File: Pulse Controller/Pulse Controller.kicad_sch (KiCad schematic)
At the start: 24 parts, among them J1 Serial, J2 RGB LED, J3 Arduino Out 1, J4 Arduino Out 2, J5 MOSFET Gates, J6 To ADC Board, P1 CONN_2, P2 PushButton, U1 ZSR330GTA, U2 ZSR500GTA, U3 4N35, U4 23LC1024

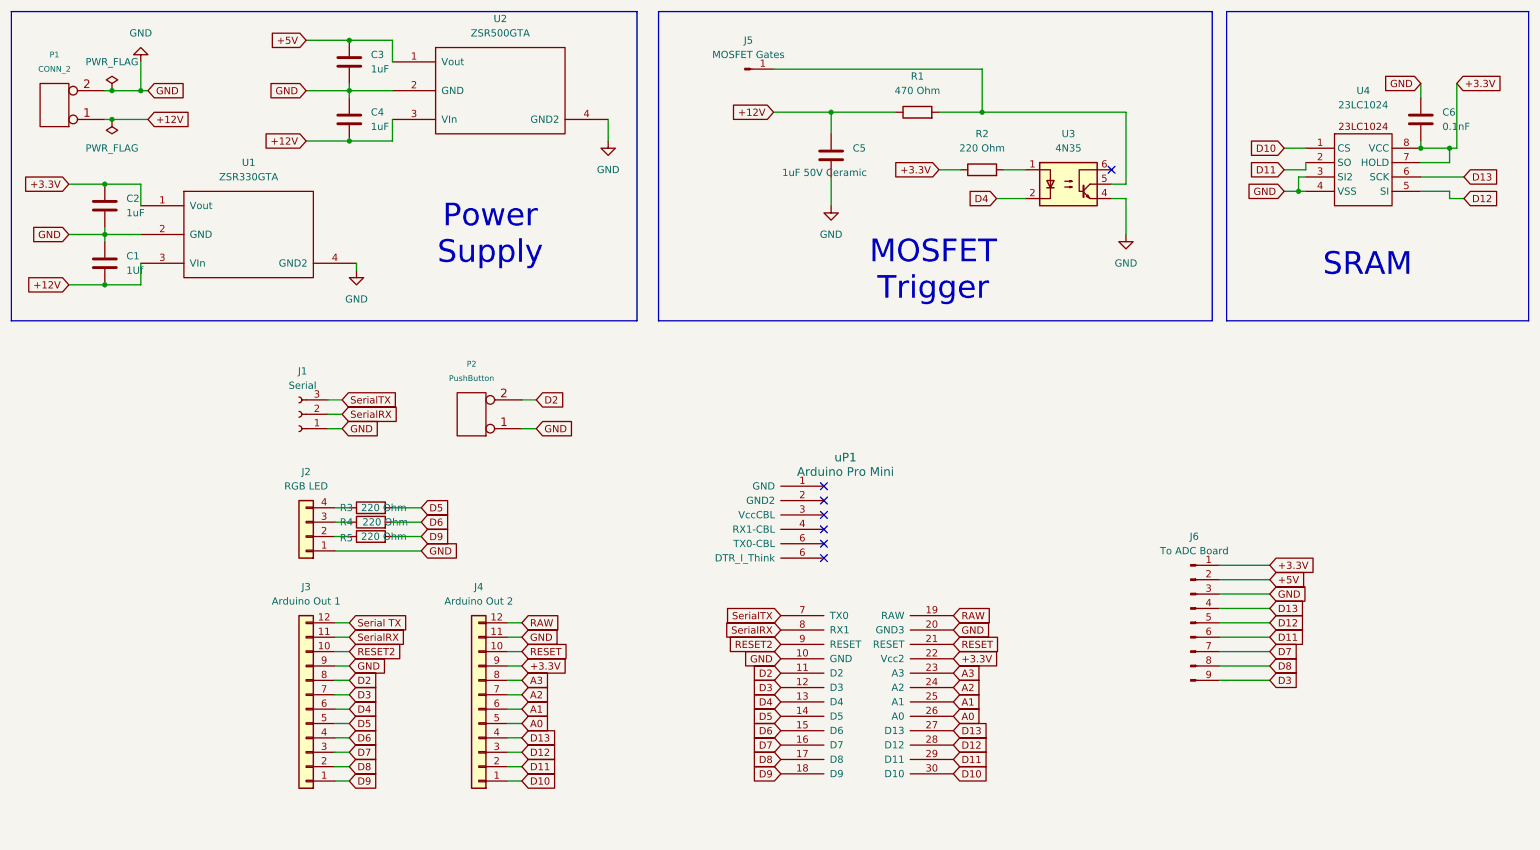
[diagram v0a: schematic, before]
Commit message: V1.0 of PPM Pulse Controller
Combined with ADC for analysis
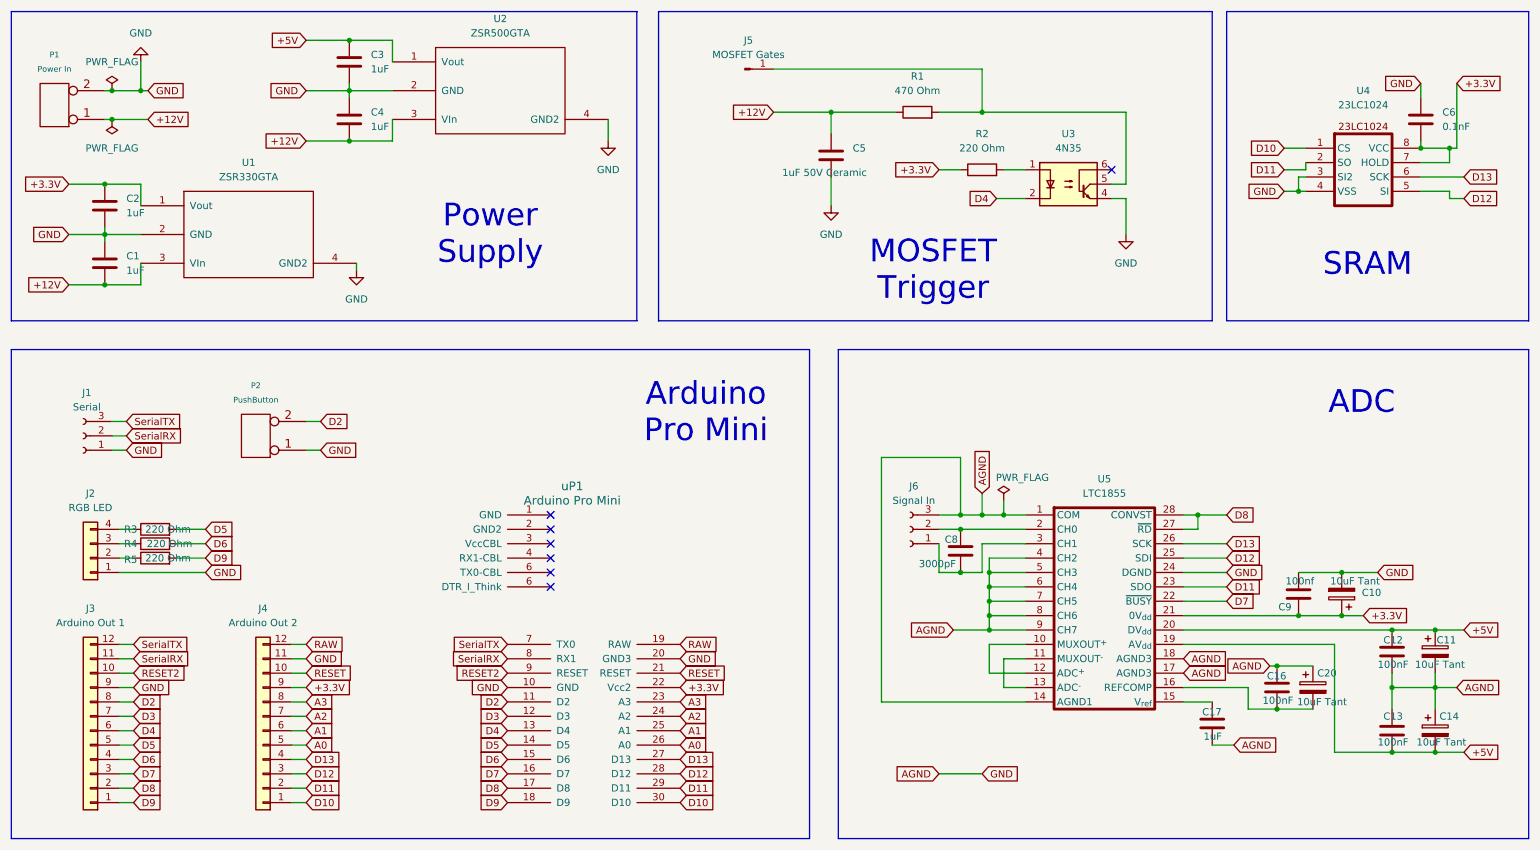
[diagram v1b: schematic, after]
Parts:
- removed J6: To ADC Board, Connector_PinHeader_2.54mm:PinHeader_1x09_P2.54mm_Vertical, symbol Connector:Conn_01x09_Pin
- added C10, C11, C14, C20: 10uF Tant, Capacitor_THT:C_Disc_D5.0mm_W2.5mm_P2.50mm, symbol Device:C_Polarized
- added C12, C13, C16: 100nF, Capacitor_SMD:C_0805_2012Metric_Pad1.18x1.45mm_HandSolder, symbol Device:C
- added C17: 1uF, Capacitor_SMD:C_0805_2012Metric_Pad1.18x1.45mm_HandSolder, symbol Device:C
- added C8: 3000pF, Capacitor_SMD:C_0805_2012Metric_Pad1.18x1.45mm_HandSolder, symbol Device:C
- added C9: 100nf, Capacitor_SMD:C_0805_2012Metric_Pad1.18x1.45mm_HandSolder, symbol Device:C
- added J6: Signal In, Connector_PinHeader_2.54mm:PinHeader_1x03_P2.54mm_Vertical, symbol Connector:Conn_01x03_Socket
- added U5: LTC1855, Package_SO:SSOP-28_5.3x10.2mm_P0.65mm, symbol DQM:LTC1855
- C1: value 1Uf -> 1uF
- C5: footprint Capacitor_THT:CP_Radial_D8.0mm_P3.50mm -> Capacitor_THT:C_Disc_D5.0mm_W2.5mm_P2.50mm
- J5: footprint DQM:PIN_ARRAY_1 -> Connector_PinHeader_2.54mm:PinHeader_1x01_P2.54mm_Horizontal
- P1: value CONN_2 -> Power In
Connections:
- net Serial TX is gone; now on net SerialTX: J3.12 (Pin_12)
- net +3.3V: now also C10.1, C9.2, U5.21 (0V_{dd})
- net +5V: now also C11.1, C12.1, C13.2, C14.2, U5.19 (AV_{dd}), U5.20 (DV_{dd})
- net D11: now also U5.23 (SDO)
- net D12: now also U5.25 (SDI)
- net D13: now also U5.26 (SCK)
- net D7: now also U5.22 (~{BUSY})
- net D8: now also U5.27 (~{RD}), U5.28 (CONVST)
- net GND: now also C10.2, C11.2, C12.2, C13.1, C14.1, C16.1, C17.2, C20.1, C9.1, J6.3 (Pin_3), U5.1 (COM), U5.14 (AGND1), U5.17 (AGND3), U5.18 (AGND3), U5.24 (DGND), U5.4 (CH2), U5.5 (CH3), U5.6 (CH4), U5.7 (CH5), U5.8 (CH6), U5.9 (CH7)
- new net: C8.1, J6.2 (Pin_2), U5.2 (CH0)
- new net: C8.2, J6.1 (Pin_1), U5.3 (CH1)
- new net: U5.10 (MUXOUT^{+}), U5.12 (ADC^{+})
- new net: U5.11 (MUXOUT^{-}), U5.13 (ADC^{-})
- new net: C17.1, U5.15 (V_{ref})
- new net: C16.2, C20.2, U5.16 (REFCOMP)
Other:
- note added: "ADC"
- note added: "Arduino Pro Mini"
- title: PPM Pulse Controller -> PPM Pulse Controller and ADC
- moved on the sheet: J1, J2, J3, J4, P2, R3, R4, R5, uP1
